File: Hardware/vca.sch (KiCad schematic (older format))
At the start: 73 parts, among them Q1 MMBFJ177, Q2 MMBFJ177, Q3 MMBFJ177, Q4 MMBFJ177, U6 TL074

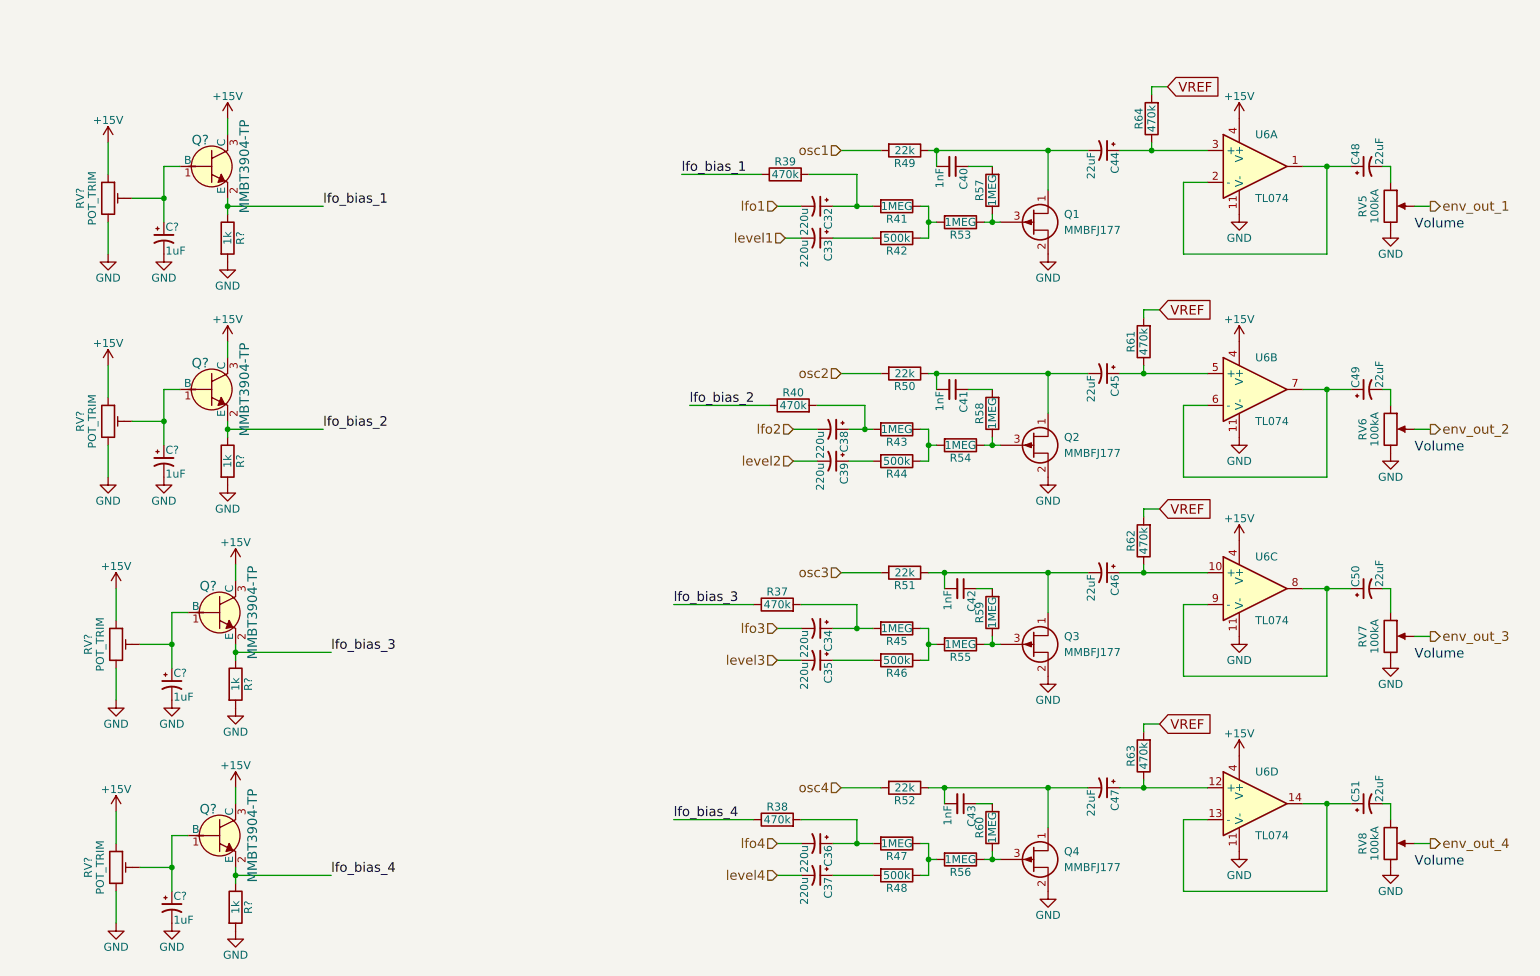
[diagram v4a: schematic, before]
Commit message: begin PCB v2 layout. fix ref designators, associate footprints on new components, create new PCB file, import components.
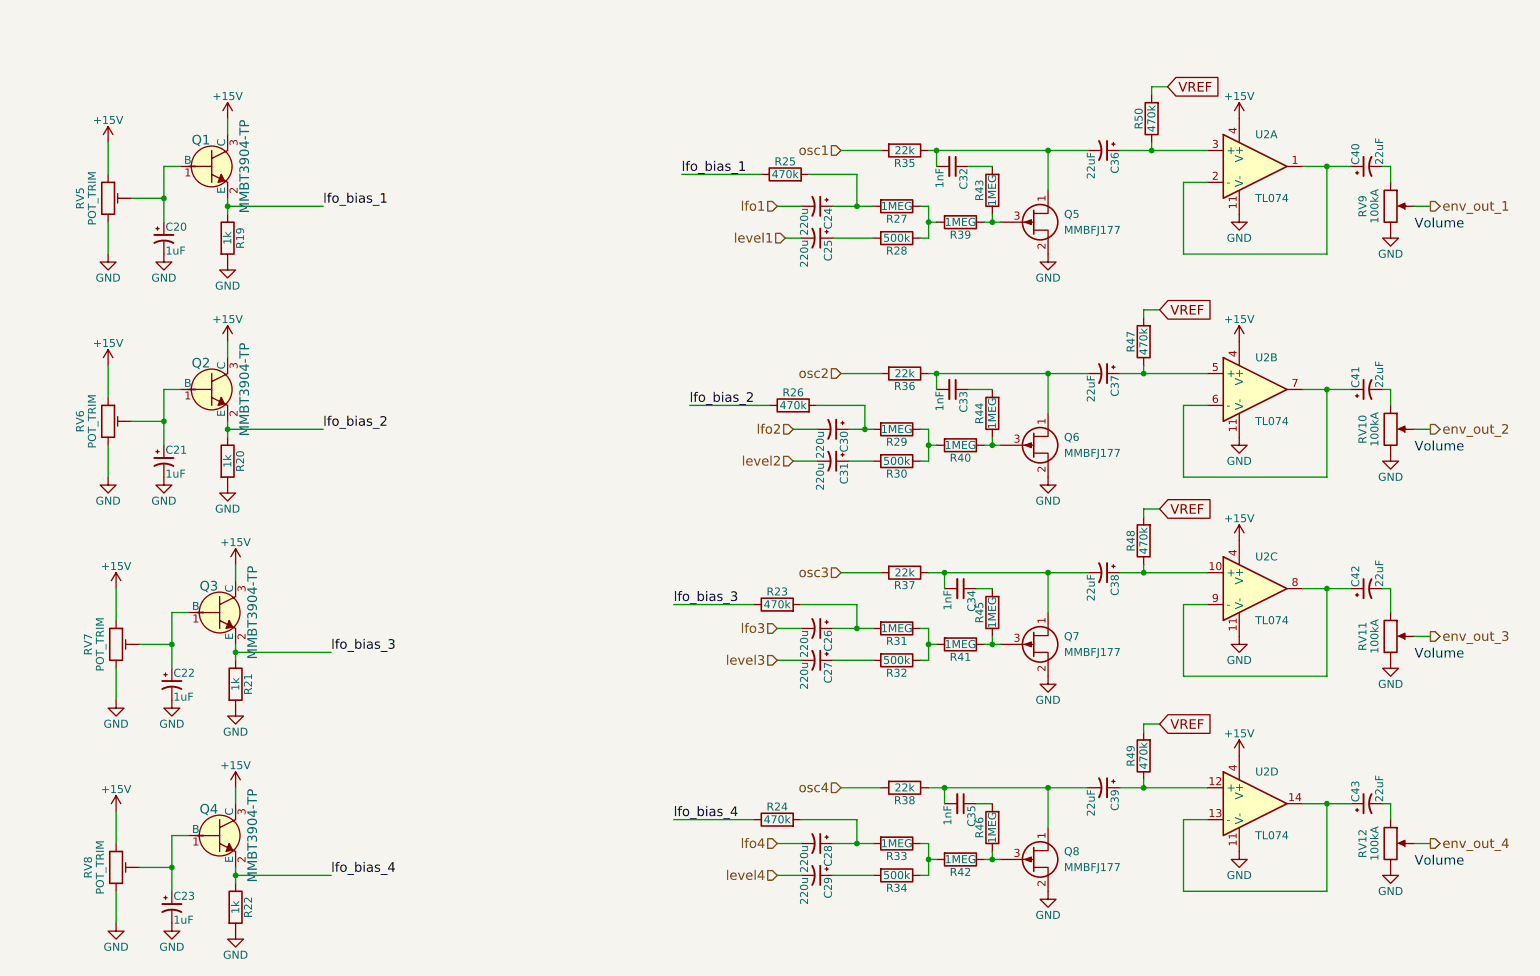
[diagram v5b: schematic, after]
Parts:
- gave numbers to parts that had none: 16
- renumbered C32 to C24, C33 to C25, C34 to C26, C35 to C27, C36 to C28, C37 to C29, C38 to C30, C39 to C31, C40 to C32, C41 to C33, C42 to C34, C43 to C35, C44 to C36, C45 to C37, C46 to C38, C47 to C39, C48 to C40, C49 to C41, C50 to C42, C51 to C43, Q1 to Q5, Q2 to Q6, Q3 to Q7, Q4 to Q8, R37 to R23, R38 to R24, R39 to R25, R40 to R26, R41 to R27, R42 to R28, R43 to R29, R44 to R30, R45 to R31, R46 to R32, R47 to R33, R48 to R34, R49 to R35, R50 to R36, R51 to R37, R52 to R38, R53 to R39, R54 to R40, R55 to R41, R56 to R42, R57 to R43, R58 to R44, R59 to R45, R60 to R46, R61 to R47, R62 to R48, R63 to R49, R64 to R50, RV6 to RV10, RV7 to RV11, RV8 to RV12, RV5 to RV9, U6 to U2
